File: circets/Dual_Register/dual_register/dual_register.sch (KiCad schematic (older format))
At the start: 22 parts

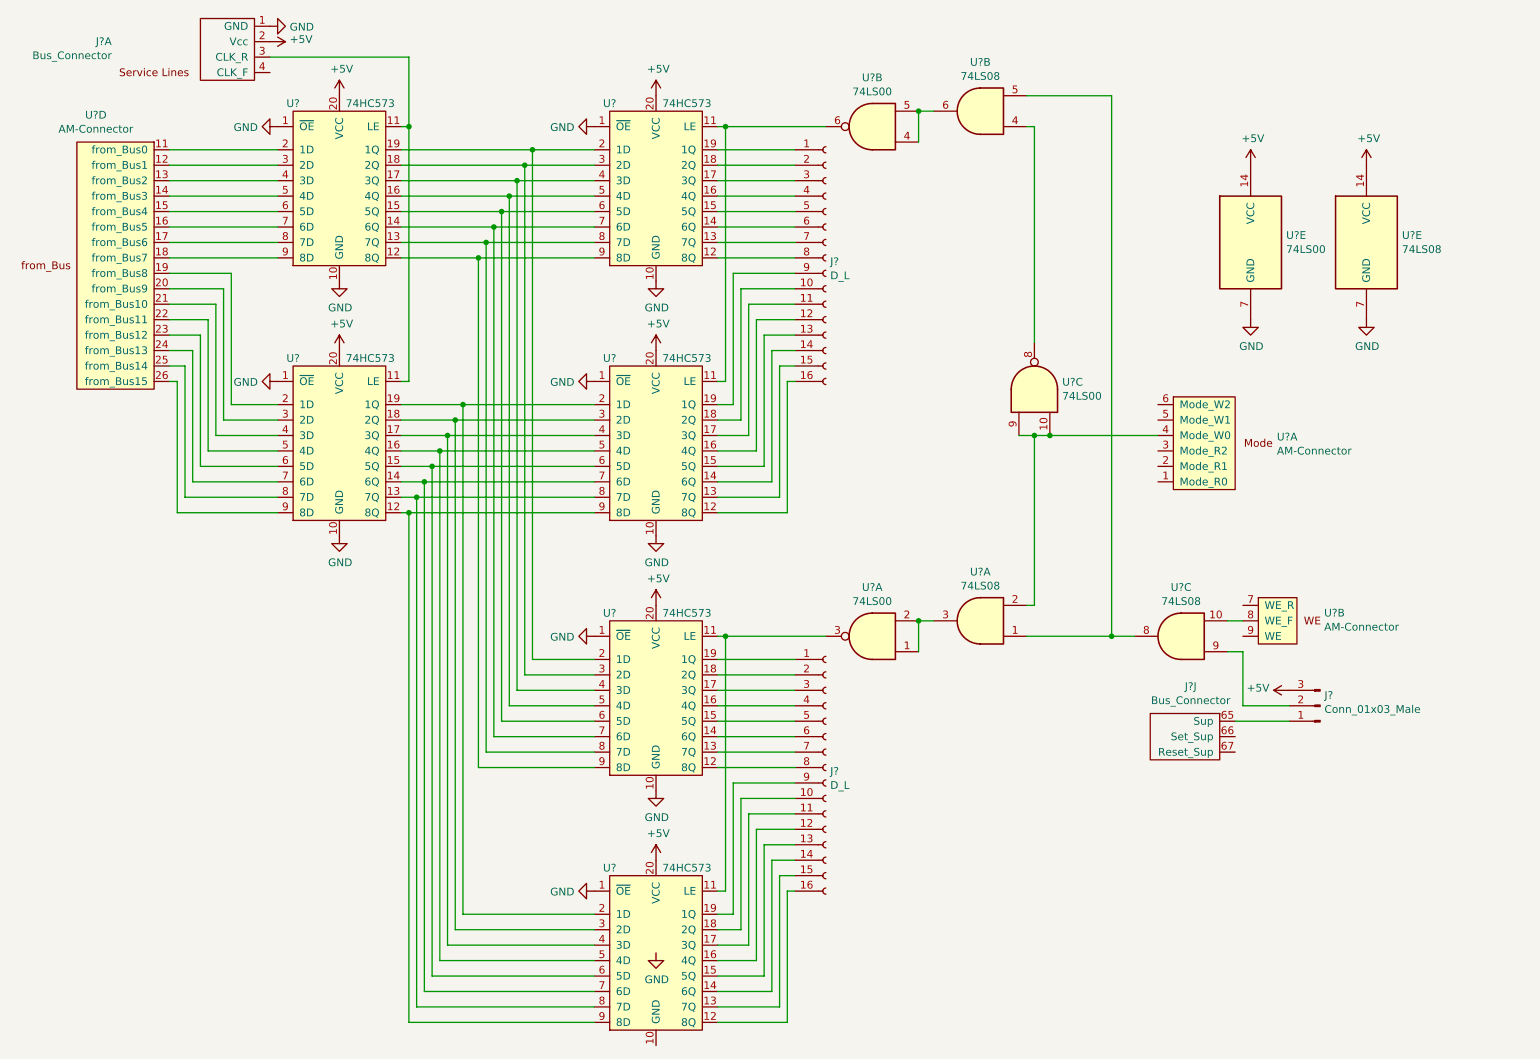
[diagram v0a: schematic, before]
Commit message: Build PCB Layout for dual Register
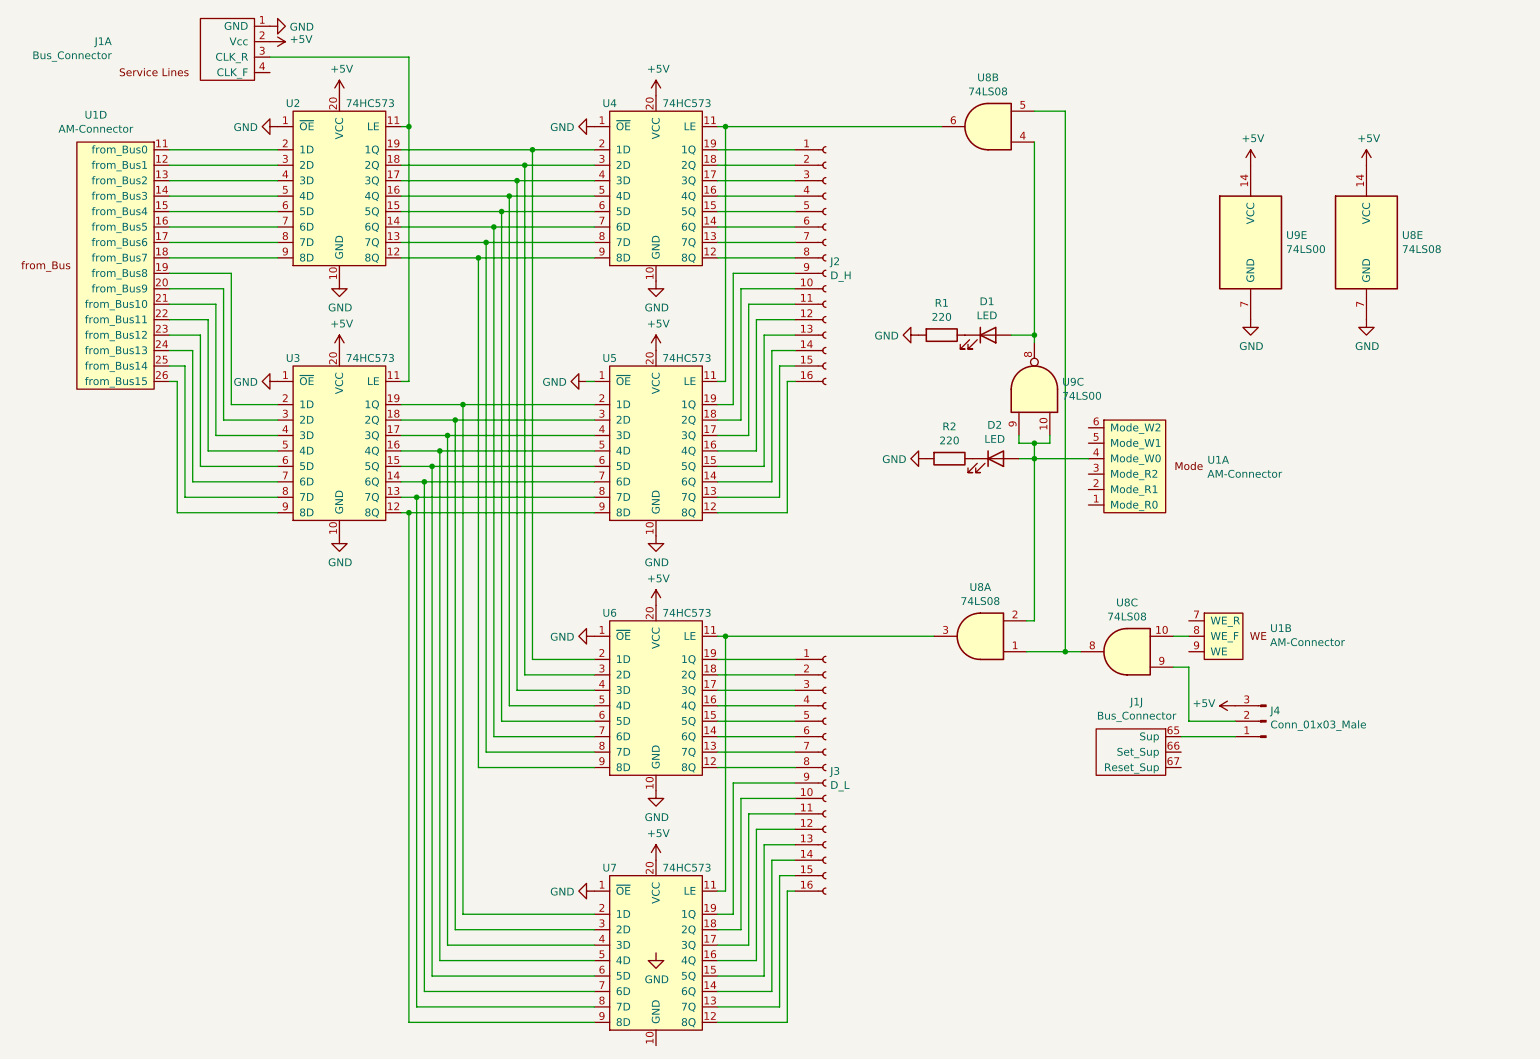
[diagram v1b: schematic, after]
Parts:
- removed U? (x2): 74LS00, symbol 74xx:74LS00
- removed U?: 74LS08, symbol 74xx:74LS08
- added D1, D2: LED, symbol Device:LED
- added R1, R2: 220, symbol Device:R
- added unit 3 of U8
- J1: renamed from J?; footprint (none) -> Computer_Component_Library:PinSocket_1x78_P2.00mm_Horizontal
- J2: renamed from J?; value D_L -> D_H; footprint (none) -> Connector_PinHeader_2.00mm:PinHeader_1x16_P2.00mm_Vertical
- J3: renamed from J?; footprint (none) -> Connector_PinHeader_2.00mm:PinHeader_1x16_P2.00mm_Vertical
- J4: renamed from J?; footprint (none) -> Connector_PinSocket_2.00mm:PinSocket_1x03_P2.00mm_Vertical
- U1: renamed from U?; footprint (none) -> Computer_Component_Library:PinSocket_1x42_P2.00mm_Horizontal
- U2, U3, U4, U5, U6, U7: renamed from U?; footprint (none) -> Package_DIP:DIP-20_W7.62mm_Socket
- U8, U9: renamed from U?; footprint (none) -> Package_DIP:DIP-14_W7.62mm_Socket
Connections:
- net GND: now also R1.2, R2.2
- net at U1.8 (WE_F): now also U8.10
- net at U6.11 (LE), U7.11 (LE): now also U8.3
- net at J4.2 (Pin_2): now also U8.9
- net at U4.11 (LE), U5.11 (LE): now also U8.6
- net at U1.4 (Mode_W0), U8.2, U9.10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: now also D2.2 (A)
- net at U8.1, U8.5: now also U8.8
- net at U8.4, U9.8: now also D1.2 (A)
- new net: D2.1 (K), R2.1
- new net: D1.1 (K), R1.1
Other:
- moved on the sheet: J1J, J4, U1A, U1B, U8A, U8B

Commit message: Enlarge Via Size
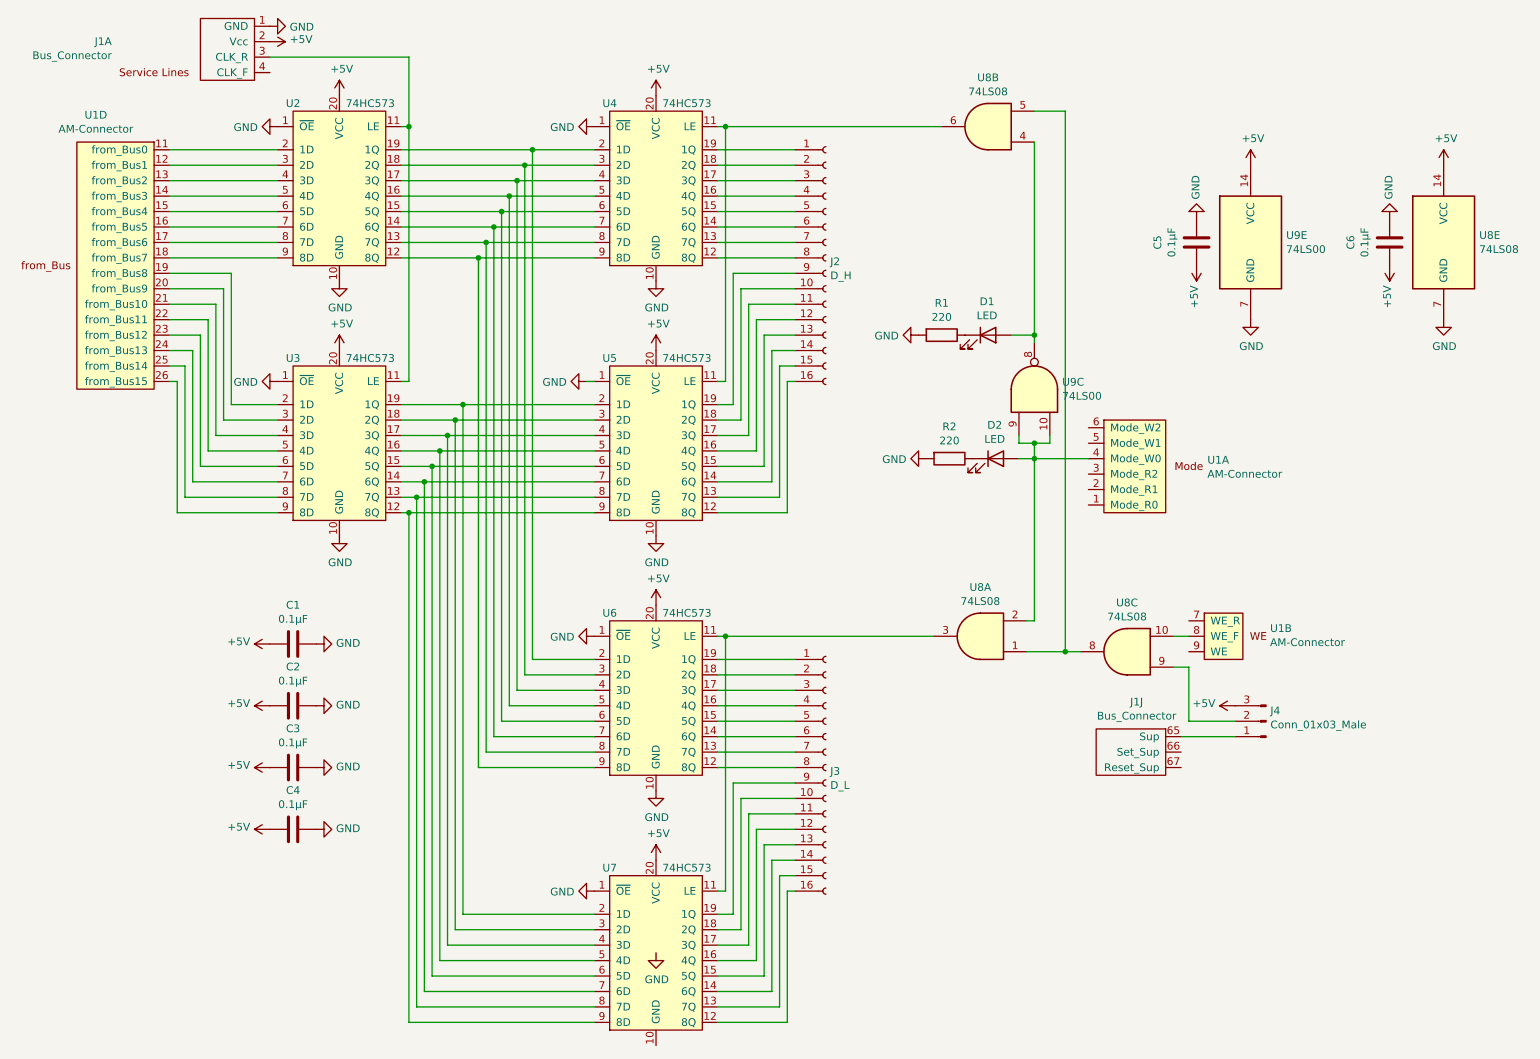
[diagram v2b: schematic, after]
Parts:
- added C1, C2, C3, C4, C5, C6: 0.1µF, Capacitor_THT:C_Disc_D8.0mm_W5.0mm_P5.00mm, symbol Device:C
- D1, D2: footprint (none) -> LED_THT:LED_D5.0mm
- J1: footprint Computer_Component_Library:PinSocket_1x78_P2.00mm_Horizontal -> Computer_Component_Library:PinHeader_1x78_P2.54mm_Horizontal
- R1, R2: footprint (none) -> Resistor_THT:R_Axial_DIN0309_L9.0mm_D3.2mm_P2.54mm_Vertical
- U1: footprint Computer_Component_Library:PinSocket_1x42_P2.00mm_Horizontal -> Computer_Component_Library:PinHeader_1x42_P2.54mm_Horizontal
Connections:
- net +5V: now also C1.2, C2.2, C3.2, C4.2, C5.2, C6.2
- net GND: now also C1.1, C2.1, C3.1, C4.1, C5.1, C6.1
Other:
- moved on the sheet: U8E
